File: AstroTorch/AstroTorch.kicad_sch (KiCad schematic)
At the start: 5 parts, among them U1 MCP1703Ax-330xxTT, U2 ATtiny24A-SS

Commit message: Next version
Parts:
- added D1, D2, D3, D4: LED WT, LED_THT:LED_D5.0mm, symbol Device:LED
- added D5, D6, D7, D8: LED RD, LED_THT:LED_D5.0mm, symbol Device:LED
- added J1: Conn_01x02_Pin, Connector_PinHeader_2.54mm:PinHeader_1x02_P2.54mm_Vertical, symbol Connector:Conn_01x02_Pin
- added Q1, Q2: IRLML2060, Package_TO_SOT_SMD:SOT-23, symbol Transistor_FET:IRLML2060
- added R1, R2, R3, R4: 100, Resistor_SMD:R_0805_2012Metric, symbol Device:R
- added R5, R6: 220, Resistor_SMD:R_0805_2012Metric, symbol Device:R
- added SW1: RotaryEncoder_Switch, Rotary_Encoder:RotaryEncoder_Alps_EC11E-Switch_Vertical_H20mm, symbol Device:RotaryEncoder_Switch
- C1, C2, C3: footprint 0805 -> Capacitor_SMD:C_0805_2012Metric
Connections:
- net +3.3V: now reaches C2.1, C3.1, U1.2 (VO), U2.1 (VCC)
- net at U2.11 (PA2): now also SW1.S2
- net at U2.12 (PA1): now also SW1.B
- net at U2.13 (AREF/PA0): now also SW1.A
- net GND: now reaches C1.2, C2.2, C3.2, U1.1 (GND), U2.14 (GND)
- net GND: now also J1.2 (Pin_2), Q1.2 (S), Q2.2 (S), SW1.C, SW1.S1
- net at U2.7 (PA6): now also R2.1
- net at U2.8 (PA5): now also R1.1
- net +9V: now reaches C1.1, U1.3 (VI)
- net +9V: now also D2.2 (A), D4.2 (A), D6.2 (A), D8.2 (A), J1.1 (Pin_1)
- new net: D3.2 (A), D4.1 (K)
- new net: Q1.1 (G), R1.2
- new net: Q1.3 (D), R3.1, R4.1
- new net: D5.1 (K), R6.2
- new net: D5.2 (A), D6.1 (K)
- new net: D1.2 (A), D2.1 (K)
- new net: D1.1 (K), R3.2
- new net: Q2.3 (D), R5.1, R6.1
- new net: D7.1 (K), R5.2
- new net: D7.2 (A), D8.1 (K)
- new net: Q2.1 (G), R2.2
- new net: D3.1 (K), R4.2

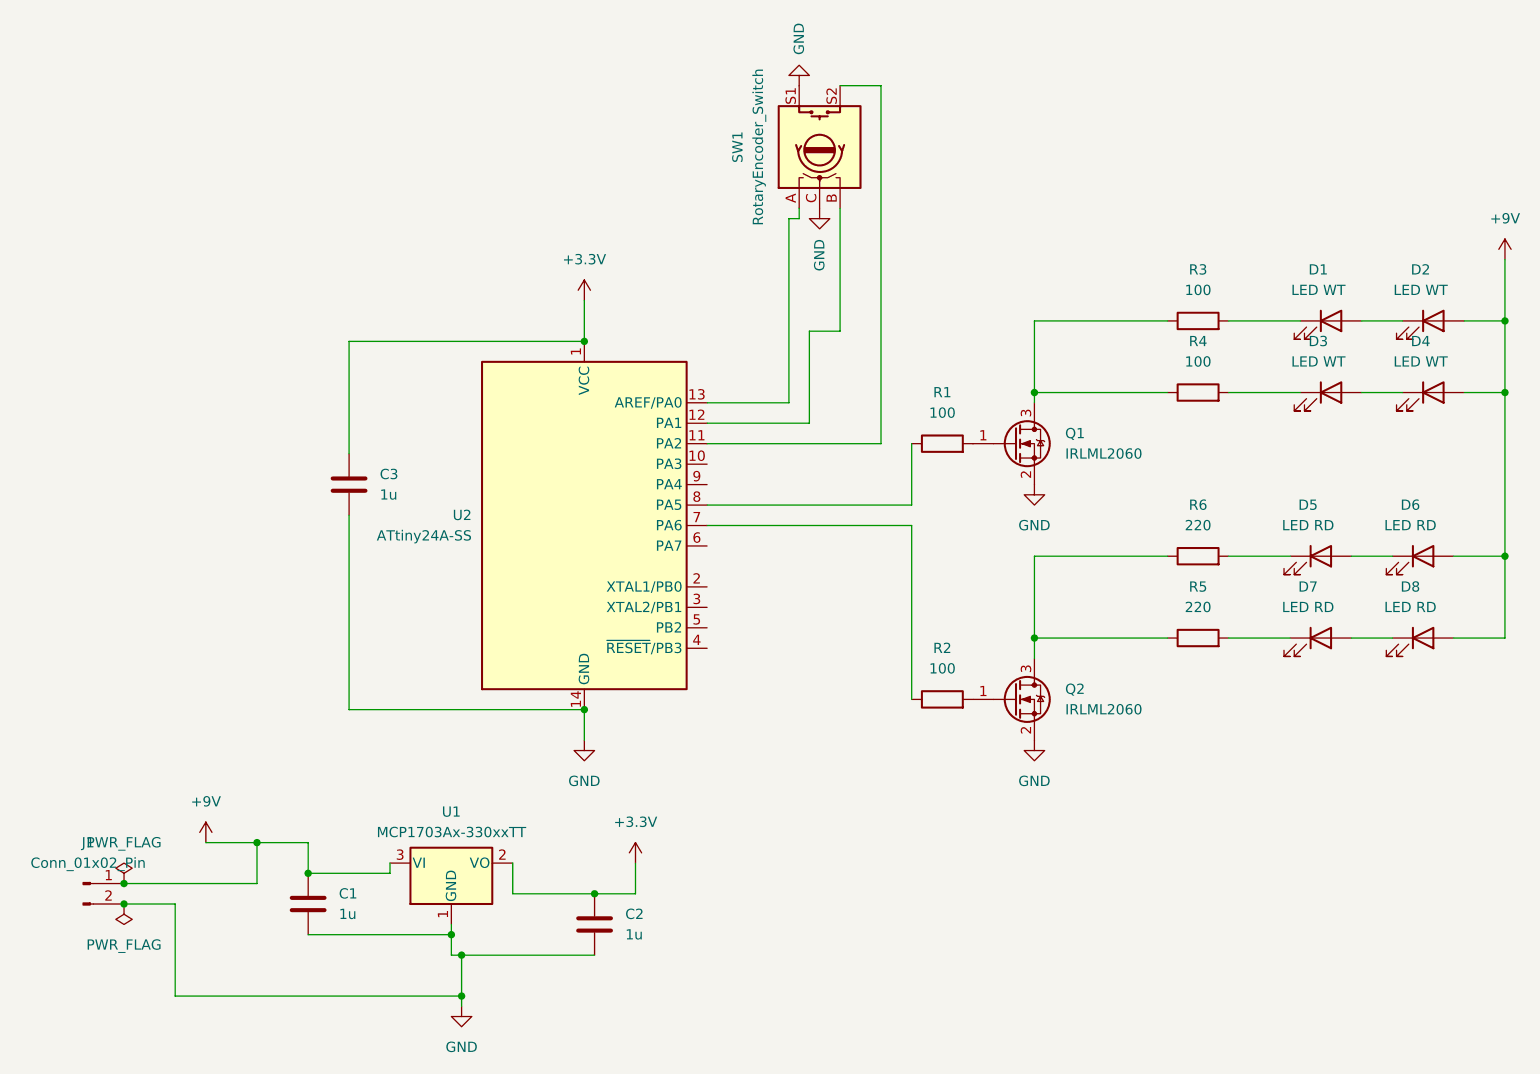
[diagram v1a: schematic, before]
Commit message: Added case
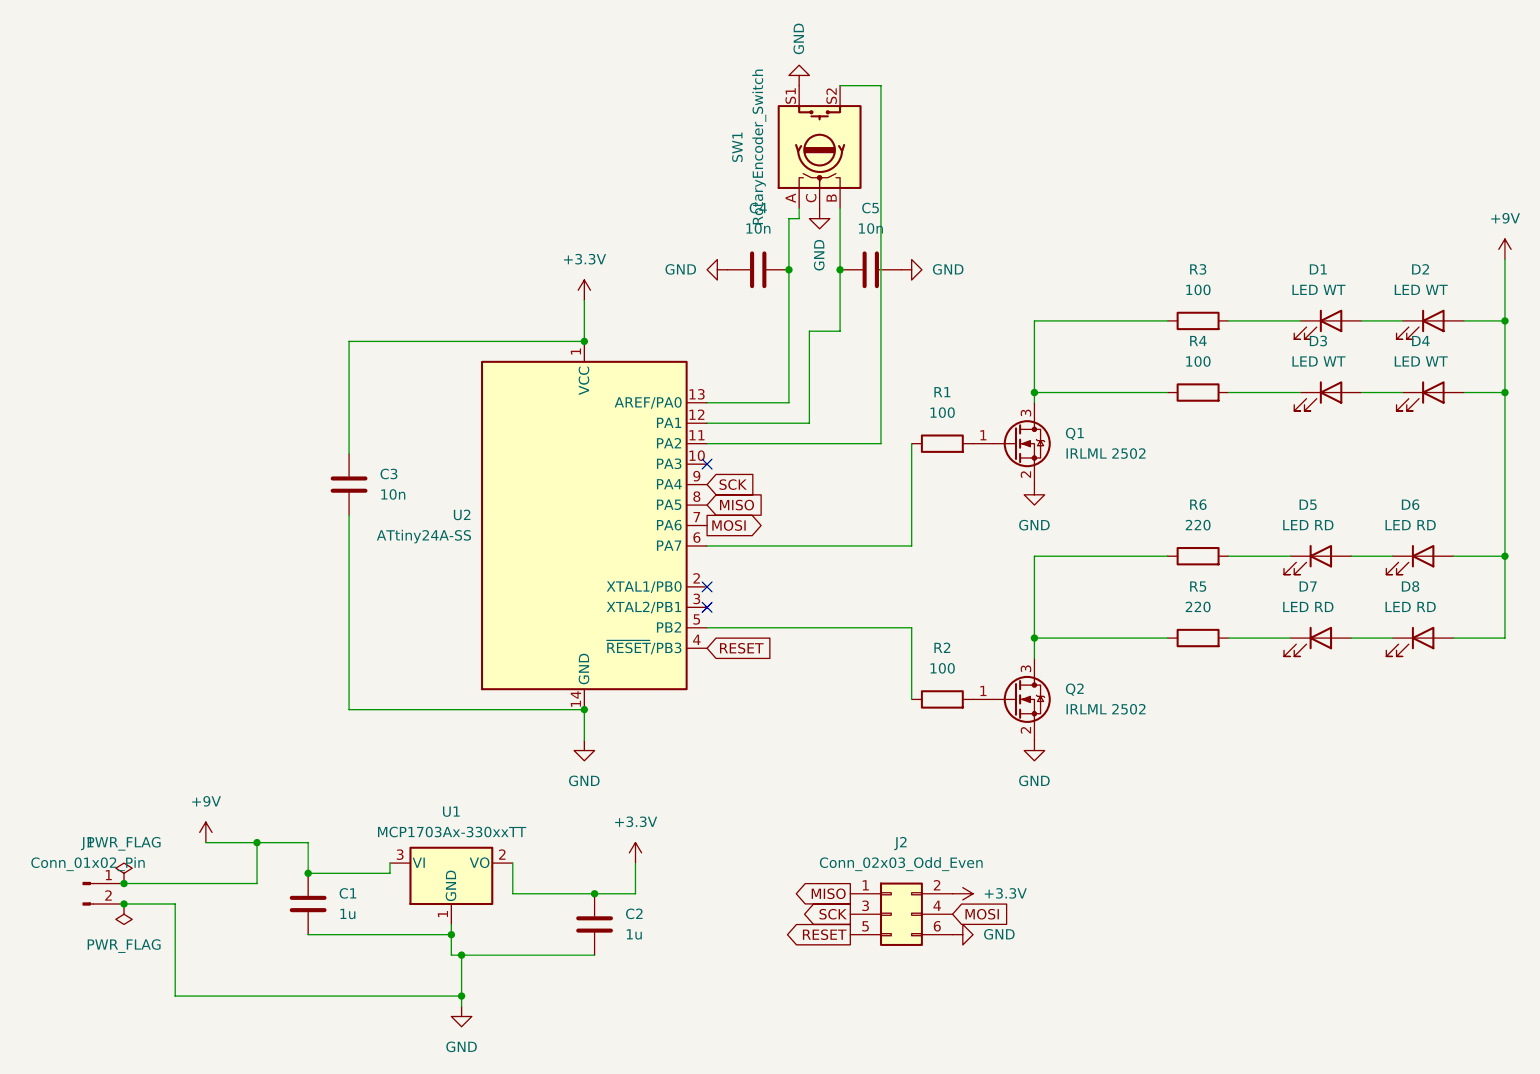
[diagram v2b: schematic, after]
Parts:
- added C4, C5: 10n, Capacitor_SMD:C_0805_2012Metric, symbol Device:C
- added J2: Conn_02x03_Odd_Even, Connector_PinHeader_2.54mm:PinHeader_2x03_P2.54mm_Vertical_SMD, symbol Connector_Generic:Conn_02x03_Odd_Even
- C3: value 1u -> 10n
- Q1, Q2: value IRLML2060 -> IRLML 2502
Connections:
- net +3.3V: now also J2.2 (Pin_2)
- net GND: now also C4.1, C5.2, J2.6 (Pin_6)
- net at R1.1: now also U2.6 (PA7); no longer U2.8 (PA5)
- net at SW1.B, U2.12 (PA1): now also C5.1
- net at SW1.A, U2.13 (AREF/PA0): now also C4.2
- net RESET: now reaches U2.4 (~{RESET}/PB3)
- net RESET: now also J2.5 (Pin_5)
- net at U2.5 (PB2): now also R2.1
- net MOSI: now reaches U2.7 (PA6)
- net MOSI: now also J2.4 (Pin_4); no longer R2.1
- net SCK: now reaches U2.9 (PA4)
- net SCK: now also J2.3 (Pin_3)
- new net MISO: J2.1 (Pin_1), U2.8 (PA5)
- no-connect marks 0 -> 3
